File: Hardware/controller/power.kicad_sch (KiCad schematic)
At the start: 32 parts

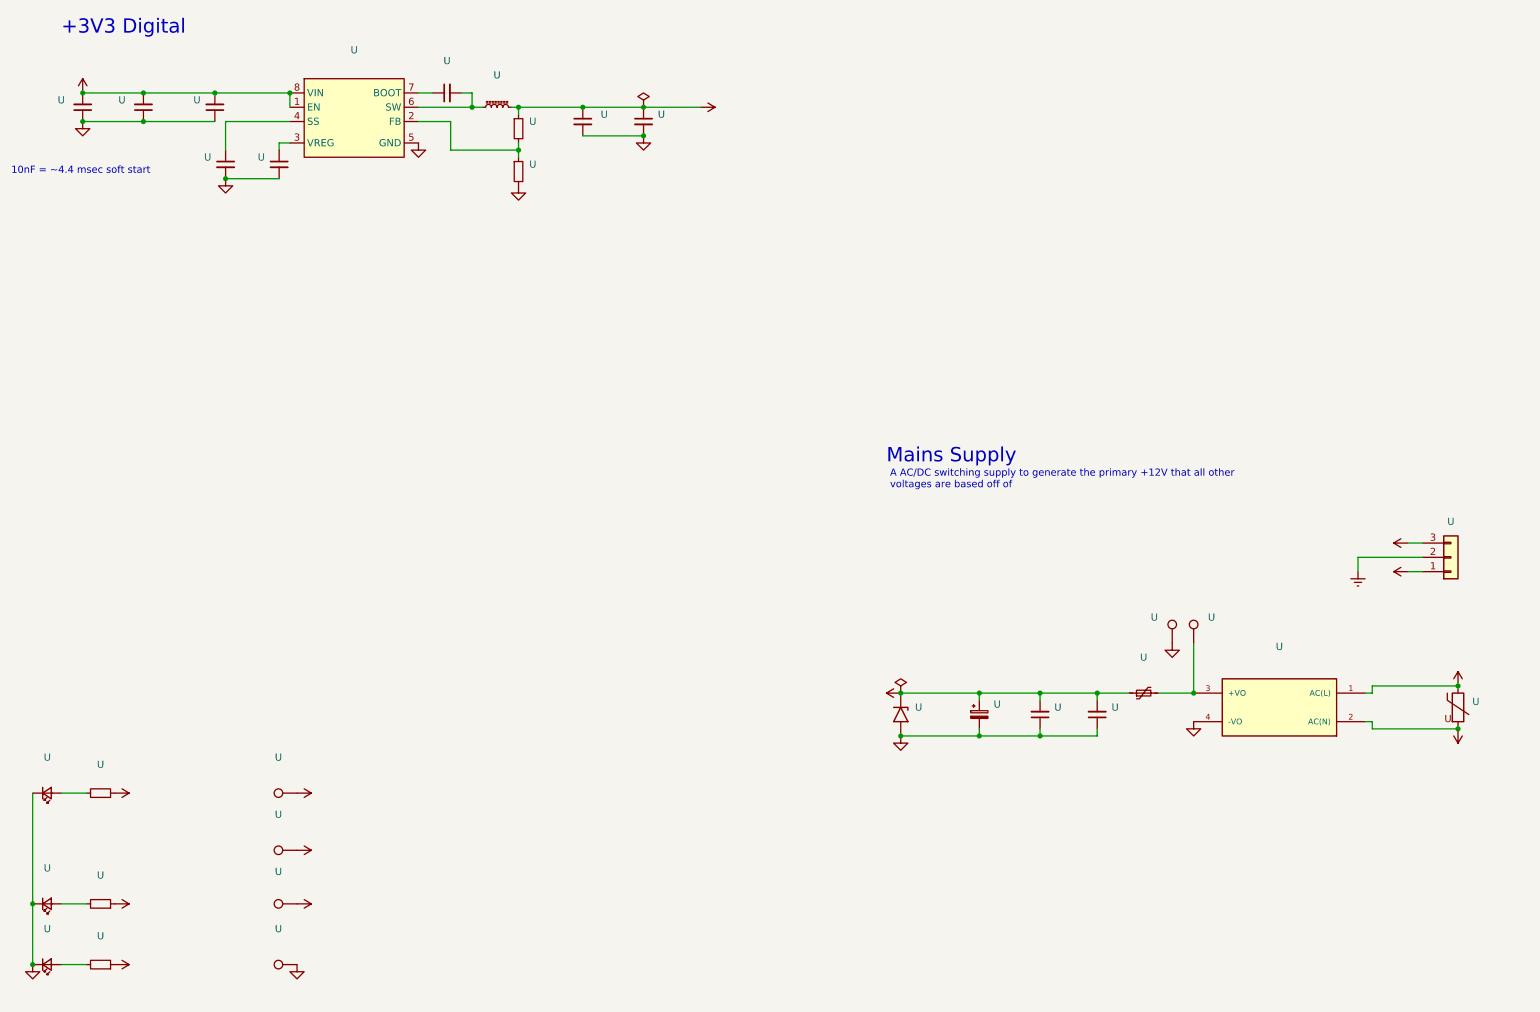
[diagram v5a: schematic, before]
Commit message: More rework of controller
- Updated power section to use a transformer + DC/DC modules, rather
  than a switching AC/DC supply: this should result in fewer bits of
  random noise floating around

- Moved a bunch of stuff around, and changed pinouts slightly of
  external connectors

- Start work on removing dependency on rear IO board

- Minor tweaks to part numbers on front panel board
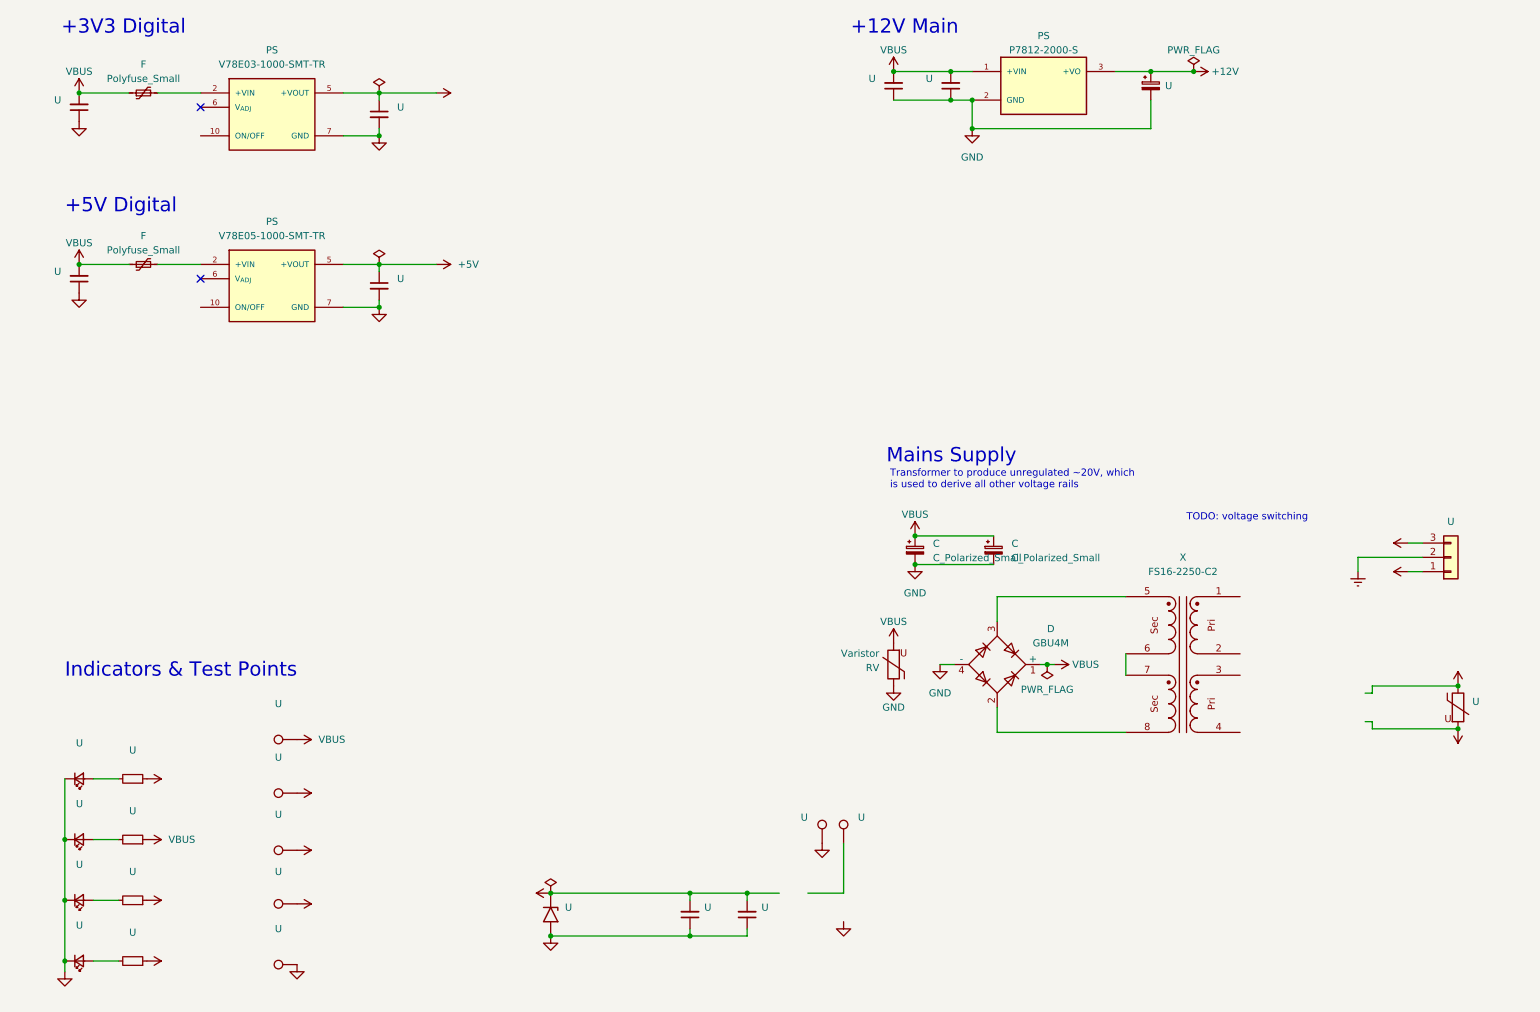
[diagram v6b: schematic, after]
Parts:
- removed U: (no value), symbol programmable-load:PSK-30D-12
- removed U (x6): (no value), symbol Device:C_Small
- removed U (x2): (no value), symbol Device:R_Small
- removed U: (no value), symbol Device:Polyfuse_Small
- removed U: (no value), symbol Device:L_Ferrite_Small
- removed U: (no value), symbol programmable-load:BD9D321EFJ
- added C (x2): C_Polarized_Small, symbol Device:C_Polarized_Small
- added D: GBU4M, Diode_THT:Diode_Bridge_Vishay_GBU, symbol Diode_Bridge:GBU4M
- added F (x2): Polyfuse_Small, symbol Device:Polyfuse_Small
- added PS: V78E03-1000-SMT-TR, programmable-load:CONV_V78E03-1000-SMT-TR, symbol programmable-load:V78E03-1000-SMT-TR
- added PS: V78E05-1000-SMT-TR, programmable-load:CONV_V78E03-1000-SMT-TR, symbol programmable-load:V78E05-1000-SMT-TR
- added PS: P7812-2000-S, programmable-load:CONV_P7812-2000-S, symbol programmable-load:P7812-2000-S
- added RV: Varistor, symbol Device:Varistor
- added U: (no value), symbol Device:R_Small
- added U: (no value), symbol Device:LED_Small
- added U: (no value), symbol Connector:TestPoint
- added U (x4): (no value), symbol Device:C_Small
- added X: FS16-2250-C2, programmable-load:Triad-FS16-2250-C2, symbol programmable-load:FS20-1800-C2
- U: MPN TMK212BBJ106KG-T -> GRM21BR61H106KE43K
- U: MPN 865060343004 -> A768EB107M1ELAE036
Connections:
- net +12V: now also PS.3 (+VO); no longer U.2
- net +3V3: now also PS.4 (+VOUT), PS.5 (+VOUT)
- net +5V: now also PS.4 (+VOUT), PS.5 (+VOUT), U.1
- net GND: now also C.2, C.2, D.4 (-), PS.2 (GND), PS.3 (GND), PS.3 (GND), PS.7 (GND), PS.7 (GND), RV.1, U.1, U.1, U.1, U.1 (K), U.2
- new net: F.2, PS.1 (+VIN), PS.2 (+VIN) (x2)
- new net: U.2, U.2 (A)
- new net: D.2, X.8
- new net: D.3, X.5
- new net: X.6, X.7
- new net VBUS: C.1, C.1, D.1 (+), F.1, F.1, PS.1 (+VIN), RV.2, U.1, U.1, U.2, U.2, U.2, U.2
- no-connect marks 0 -> 2
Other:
- note added: "+12V Main"
- note added: "+5V Digital"
- note added: "Indicators & Test Points"
- note added: "TODO: voltage switching"
- note added: "Transformer to produce unregulated ~20V, which is used to derive all other voltage rails"
- note removed: "10nF = ~4.4 msec soft start"
- note removed: "A AC/DC switching supply to generate the primary +12V that all other voltages are based off of"
- moved on the sheet: U

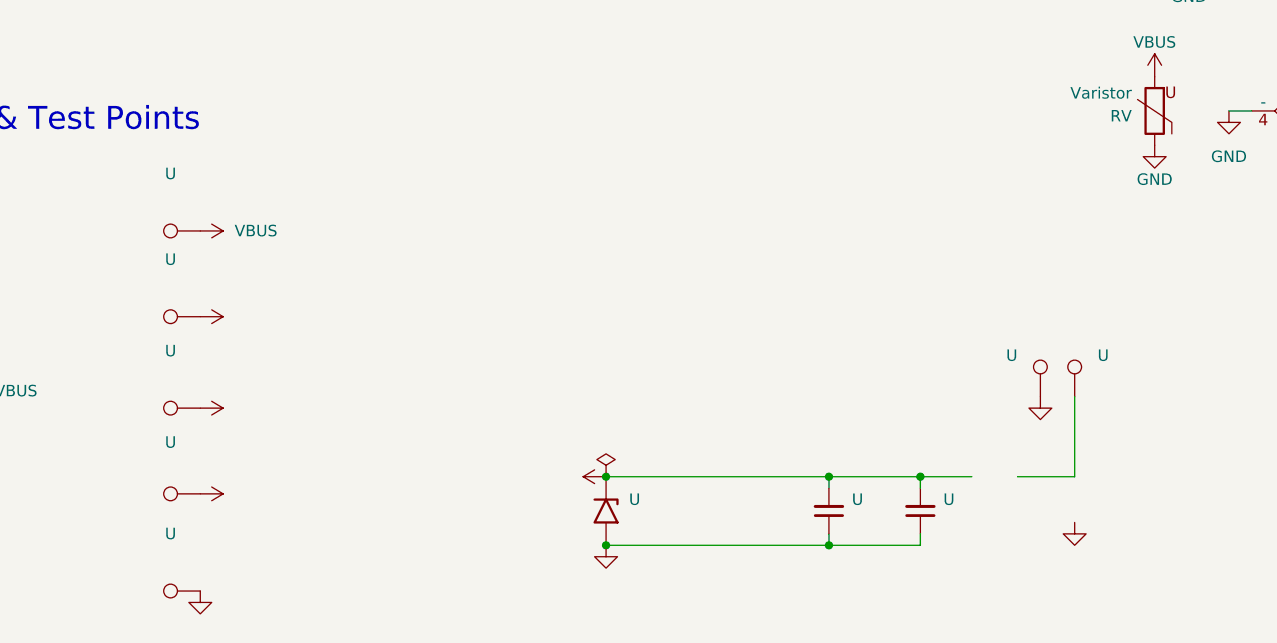
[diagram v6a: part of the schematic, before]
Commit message: More reworking of the controller and friends
- Add more rear IO to the controller, in this case finishing positioning
  of the Ethernet jack, and adding a suitable right angle USB B jack
  (USB C is preferrable but there's basically no jacks that are
  sufficiently long)

- Mostly finish power section on controller (save for the enable input
  for our +3V3 rail; it'll be slaved off the SoM +3V3 rail)

- Minor tweaks to pinout of FFC connector on front panel

- Update cutout shape of analog board

- Fixed a few footprints metadata

- Add footprints for further rear panel IO
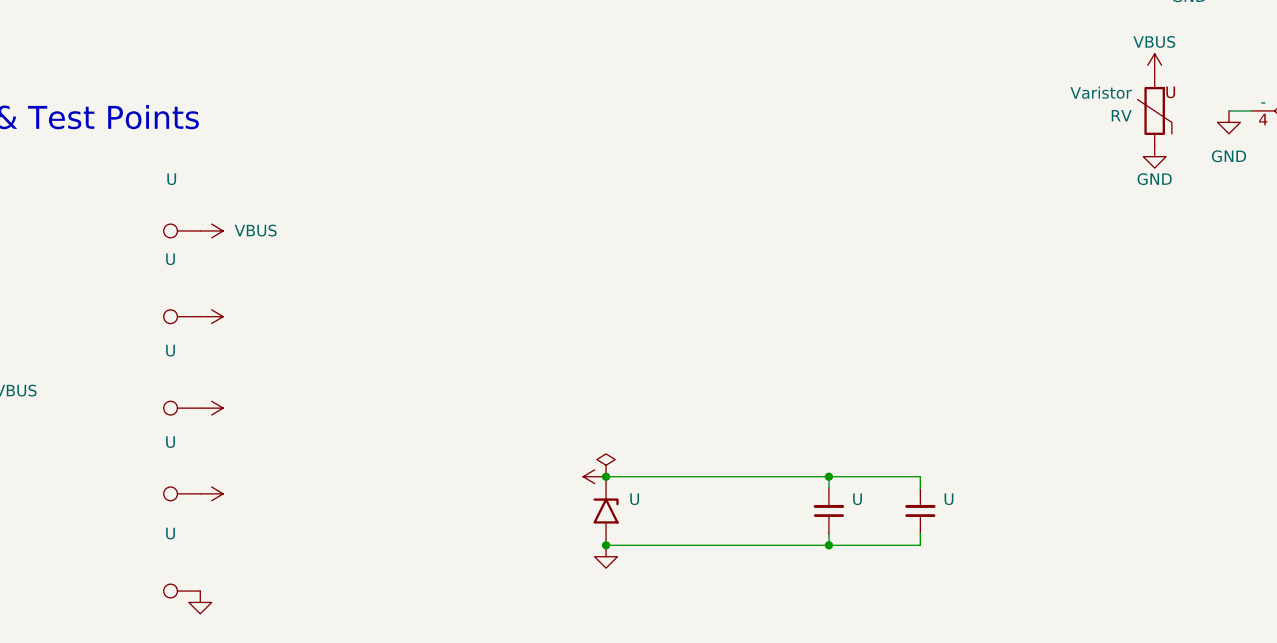
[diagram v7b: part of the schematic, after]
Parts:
- removed U (x2): (no value), symbol Connector:TestPoint
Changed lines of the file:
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@@
   (junction (at 27.94 35.56) (diameter 0) (color 0 0 0 0)
-  )
-  (junction (at 146.685 177.8) (diameter 0) (color 0 0 0 0)
   )
   (junction (at 186.69 41.91) (diameter 0) (color 0 0 0 0)
@@
     (stroke (width 0) (type default))
   )
-  (wire (pts (xy 157.48 177.8) (xy 163.83 177.8))
-    (stroke (width 0) (type default))
-  )
   (wire (pts (xy 30.48 179.07) (xy 34.925 179.07))
     (stroke (width 0) (type default))
@@
     (stroke (width 0) (type default))
   )
-  (wire (pts (xy 163.83 168.91) (xy 163.83 177.8))
-    (stroke (width 0) (type default))
-  )
   (wire (pts (xy 200.025 137.16) (xy 201.295 137.16))
     (stroke (width 0) (type default))
@@
   )
   (wire (pts (xy 213.995 149.225) (xy 191.135 149.225))
-    (stroke (width 0) (type default))
-  )
-  (wire (pts (xy 146.685 177.8) (xy 152.4 177.8))
     (stroke (width 0) (type default))
   )
@@
     (pin "1")
   )
-  (symbol (lib_id "Connector:TestPoint") (at 160.02 168.91 0) (mirror y) (unit 1)
-    (in_bom yes) (on_board yes) (fields_autoplaced)
-    (default_instance (reference "U") (unit 1) (value "") (footprint ""))
-    (property "Reference" "U" (id 0) (at 157.48 164.3379 0)
-      (effects (font (size 1.27 1.27)) (justify left))
-    )
-    (property "Value" "" (id 1) (at 157.48 166.8779 0)
-      (effects (font (size 1.27 1.27)) (justify left))
-    )
-    (property "Footprint" "" (id 2) (at 154.94 168.91 0)
-      (effects (font (size 1.27 1.27)) hide)
-    )
-    (property "Datasheet" "~" (id 3) (at 154.94 168.91 0)
-      (effects (font (size 1.27 1.27)) hide)
-    )
-    (property "MPN" "571-0100" (id 4) (at 160.02 168.91 0)
-      (effects (font (size 1.27 1.27)) hide)
-    )
-    (pin "1")
-  )
   (symbol (lib_id "power:+12V") (at 226.06 31.75 270) (unit 1)
     (in_bom yes) (on_board yes)
@@
   )
   (symbol (lib_id "Connector:TestPoint") (at 66.675 150.495 90) (mirror x) (unit 1)
-    (in_bom yes) (on_board yes) (fields_autoplaced)
-    (default_instance (reference "U") (unit 1) (value "") (footprint ""))
-    (property "Reference" "U" (id 0) (at 63.373 144.145 90)
-      (effects (font (size 1.27 1.27)))
-    )
-    (property "Value" "" (id 1) (at 63.373 146.685 90)
+    (in_bom yes) (on_board yes)
+    (default_instance (reference "U") (unit 1) (value "") (footprint ""))
+    (property "Reference" "U" (id 0) (at 63.5 144.78 90)
+      (effects (font (size 1.27 1.27)))
+    )
+    (property "Value" "" (id 1) (at 63.5 147.32 90)
       (effects (font (size 1.27 1.27)))
     )
@@
     (pin "2")
   )
-  (symbol (lib_id "power:GND") (at 160.02 168.91 0) (unit 1)
-    (in_bom yes) (on_board yes)
-    (default_instance (reference "U") (unit 1) (value "") (footprint ""))
-    (property "Reference" "U" (id 0) (at 160.02 175.26 0)
-      (effects (font (size 1.27 1.27)) hide)
-    )
-    (property "Value" "" (id 1) (at 160.02 172.72 0)
-      (effects (font (size 1.27 1.27)))
-    )
-    (property "Footprint" "" (id 2) (at 160.02 168.91 0)
-      (effects (font (size 1.27 1.27)) hide)
-    )
-    (property "Datasheet" "" (id 3) (at 160.02 168.91 0)
-      (effects (font (size 1.27 1.27)) hide)
-    )
-    (pin "1")
-  )
   (symbol (lib_id "Device:C_Small") (at 27.94 68.58 0) (mirror x) (unit 1)
     (in_bom yes) (on_board yes)
@@
     )
     (property "Datasheet" "" (id 3) (at 27.94 40.64 0)
-      (effects (font (size 1.27 1.27)) hide)
-    )
-    (pin "1")
-  )
-  (symbol (lib_id "power:GND") (at 163.83 182.88 0) (unit 1)
-    (in_bom yes) (on_board yes)
-    (default_instance (reference "U") (unit 1) (value "") (footprint ""))
-    (property "Reference" "U" (id 0) (at 163.83 189.23 0)
-      (effects (font (size 1.27 1.27)) hide)
-    )
-    (property "Value" "" (id 1) (at 163.83 186.69 0)
-      (effects (font (size 1.27 1.27)))
-    )
-    (property "Footprint" "" (id 2) (at 163.83 182.88 0)
-      (effects (font (size 1.27 1.27)) hide)
-    )
-    (property "Datasheet" "" (id 3) (at 163.83 182.88 0)
       (effects (font (size 1.27 1.27)) hide)
     )
@@
     (pin "2")
   )
-  (symbol (lib_id "Connector:TestPoint") (at 163.83 168.91 0) (unit 1)
-    (in_bom yes) (on_board yes) (fields_autoplaced)
-    (default_instance (reference "U") (unit 1) (value "") (footprint ""))
-    (property "Reference" "U" (id 0) (at 166.37 164.3379 0)
-      (effects (font (size 1.27 1.27)) (justify left))
-    )
-    (property "Value" "" (id 1) (at 166.37 166.8779 0)
-      (effects (font (size 1.27 1.27)) (justify left))
-    )
-    (property "Footprint" "" (id 2) (at 168.91 168.91 0)
-      (effects (font (size 1.27 1.27)) hide)
-    )
-    (property "Datasheet" "~" (id 3) (at 168.91 168.91 0)
-      (effects (font (size 1.27 1.27)) hide)
-    )
-    (property "MPN" "571-0200" (id 4) (at 163.83 168.91 0)
-      (effects (font (size 1.27 1.27)) hide)
-    )
-    (pin "1")
-  )
   (symbol (lib_id "power:VBUS") (at 172.72 133.35 0) (unit 1)
